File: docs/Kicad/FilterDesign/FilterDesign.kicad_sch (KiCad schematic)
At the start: 2 parts

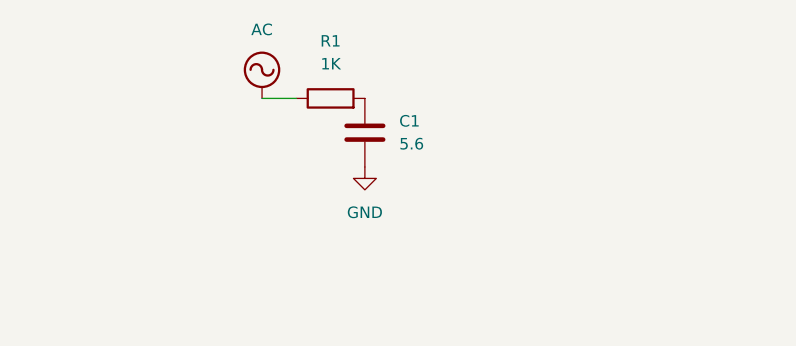
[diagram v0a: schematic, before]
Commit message: Worked on filter simulation in KiCad
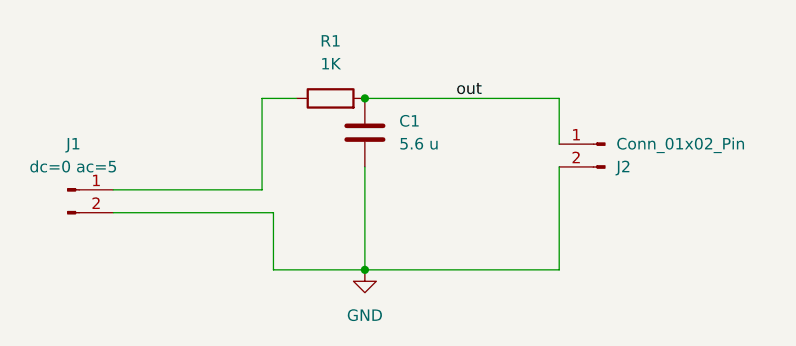
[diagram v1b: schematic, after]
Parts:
- added J1: ${SIM.PARAMS}, symbol Connector:Conn_01x02_Pin
- added J2: Conn_01x02_Pin, symbol Connector:Conn_01x02_Pin
- C1: value 5.6 -> 5.6 u
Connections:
- net GND: now also J1.2 (Pin_2), J2.2 (Pin_2)
- net out: now reaches C1.1, R1.2
- net out: now also J2.1 (Pin_1)
- net AC: no longer names the net of R1.1
- net AC: now also J1.1 (Pin_1)

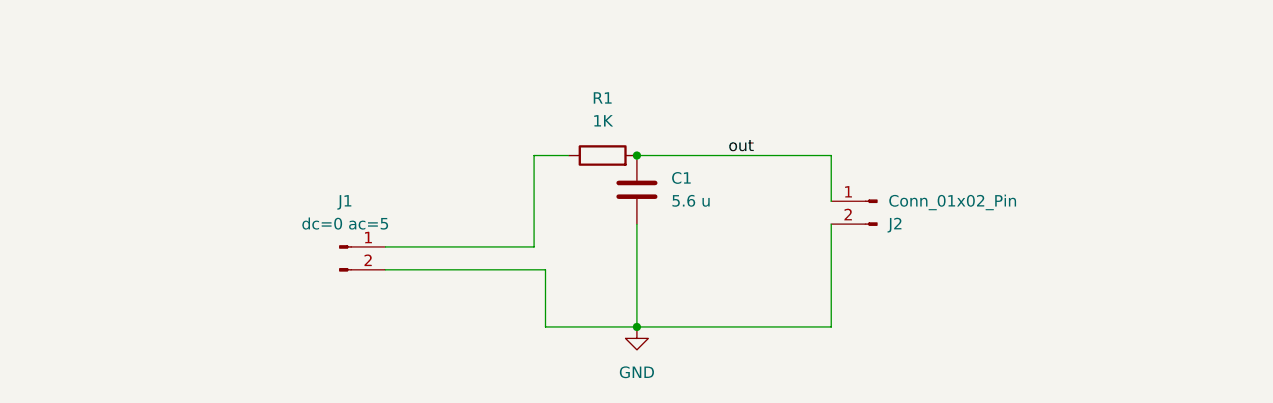
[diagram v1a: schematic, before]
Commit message: Added new README.md and worked on filter
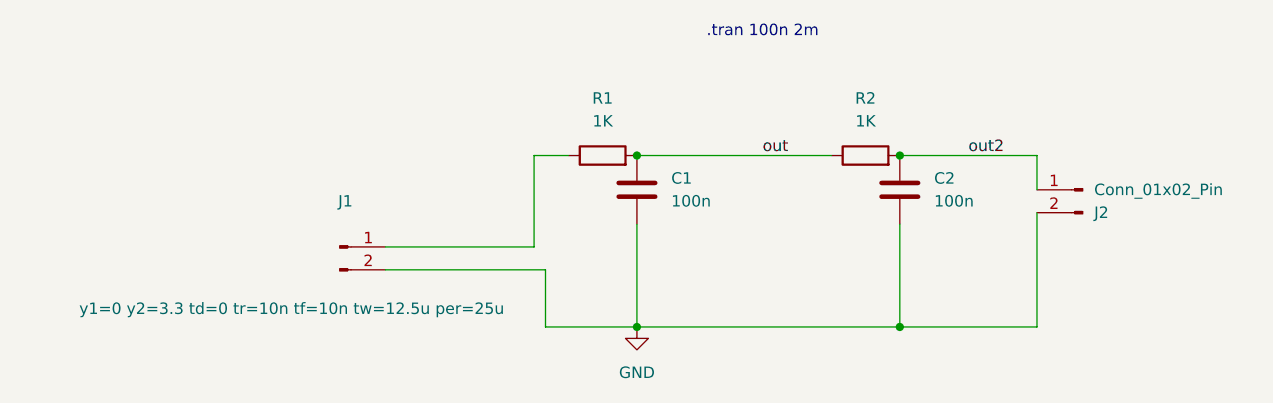
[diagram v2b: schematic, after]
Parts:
- added C2: 100n, symbol Device:C
- added R2: 1K, symbol Device:R
- C1: value 5.6 u -> 100n
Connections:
- net GND: now also C2.2
- net out: now also R2.1; no longer J2.1 (Pin_1)
- new net out2: C2.1, J2.1 (Pin_1), R2.2
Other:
- note added: ".tran 100n 2m"
- moved on the sheet: J2

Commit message: Working on Active filter
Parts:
- removed C1, C2: 100n, symbol Device:C
- removed J1: ${SIM.PARAMS}, symbol Connector:Conn_01x02_Pin
- removed J2: Conn_01x02_Pin, symbol Connector:Conn_01x02_Pin
- removed R1, R2: 1K, symbol Device:R
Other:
- added sheet Active Filter (Active_Filter.kicad_sch)
- added sheet Passive filter (Passive_filter.kicad_sch)
- note removed: ".tran 100n 2m"

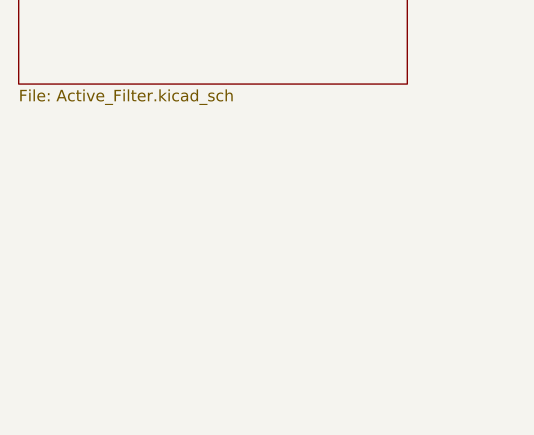
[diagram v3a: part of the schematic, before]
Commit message: Sallen-key topology low-pass filter tilføjet i kicad
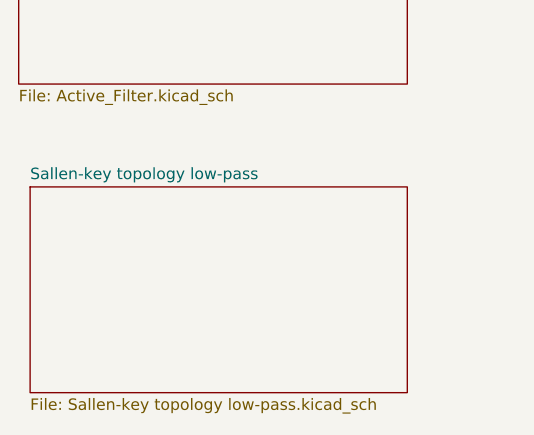
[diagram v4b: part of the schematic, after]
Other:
- added sheet Sallen-key topology low-pass (Sallen-key topology low-pass.kicad_sch)
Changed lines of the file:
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@@
 (kicad_sch
-	(version 20231120)
+	(version 20250114)
 	(generator "eeschema")
-	(generator_version "8.0")
+	(generator_version "9.0")
 	(paper "A4")
 	(sheet
 		(at 26.67 26.67)
 		(size 43.18 20.32)
+		(exclude_from_sim no)
+		(in_bom yes)
+		(on_board yes)
+		(dnp no)
 		(fields_autoplaced yes)
 		(stroke
@@
 		(at 26.67 58.42)
 		(size 43.18 19.05)
+		(exclude_from_sim no)
+		(in_bom yes)
+		(on_board yes)
+		(dnp no)
 		(fields_autoplaced yes)
 		(stroke
@@
 		)
 	)
+	(sheet
+		(at 27.94 88.9)
+		(size 41.91 22.86)
+		(exclude_from_sim no)
+		(in_bom yes)
+		(on_board yes)
+		(dnp no)
+		(fields_autoplaced yes)
+		(stroke
+			(width 0.1524)
+			(type solid)
+		)
+		(fill
+			(color 0 0 0 0.0000)
+		)
+		(property "Sheetname" "Sallen-key topology low-pass"
+			(at 27.94 88.1884 0)
+			(effects
+				(font
+					(size 1.27 1.27)
+				)
+				(justify left bottom)
+			)
+		)
+		(property "Sheetfile" "Sallen-key topology low-pass.kicad_sch"
+			(at 27.94 112.3446 0)
+			(effects
+				(font
+					(size 1.27 1.27)
+				)
+				(justify left top)
+			)
+		)
+		(instances
+			(project "FilterDesign"
+				(path "/33ea2c5c-8786-4c1d-9e9b-dd794a9e2536"
+					(page "4")
+				)
+			)
+		)
+	)
 	(sheet_instances
 		(path "/"
@@
 		)
 	)
+	(embedded_fonts no)
 )
